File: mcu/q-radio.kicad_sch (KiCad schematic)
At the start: 0 parts

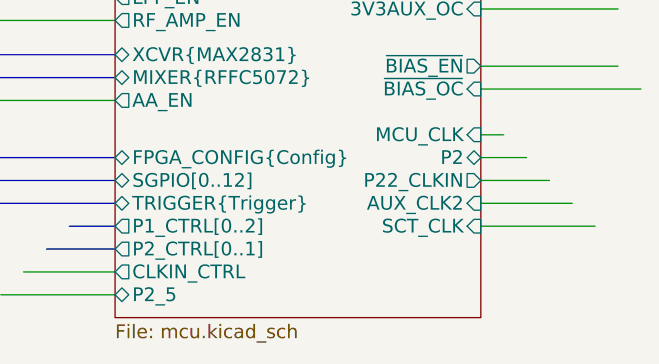
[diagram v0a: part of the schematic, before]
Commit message: separated LED and SW subcircuit as it's pre-placed and not part of MCU room. Updated all other sch subcircuits.
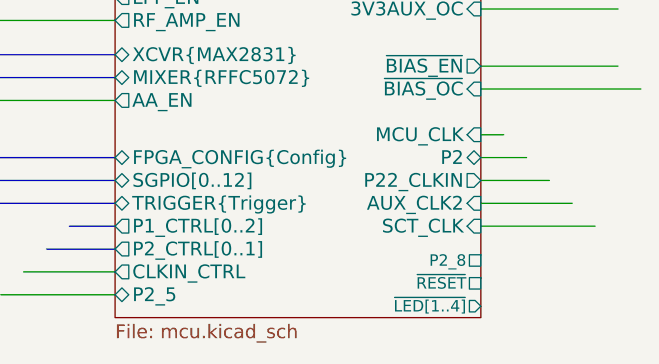
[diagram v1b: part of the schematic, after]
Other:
- sheet Microcontroller ports: added P2_8, ~{LED[1..4]}, ~{RESET}; removed none
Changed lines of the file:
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@@
+			)
+		)
+		(pin "~{LED[1..4]}" output
+			(at 226.06 83.82 0)
+			(effects
+				(font
+					(size 1.27 1.27)
+				)
+				(justify right)
+			)
+		)
+		(pin "P2_8" passive
+			(at 226.06 78.74 0)
+			(effects
+				(font
+					(size 1.27 1.27)
+				)
+				(justify right)
+			)
+		)
+		(pin "~{RESET}" passive
+			(at 226.06 81.28 0)
+			(effects
+				(font
+					(size 1.27 1.27)
+				)
+				(justify right)
 			)
 		)
